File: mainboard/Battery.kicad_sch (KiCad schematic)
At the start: 24 parts, among them IC701 USBLC6-2P6, IC702 BQ21040DBV, IC703 MAX17048, Q701 Si2333CDS, X701 USB, X702 Battery

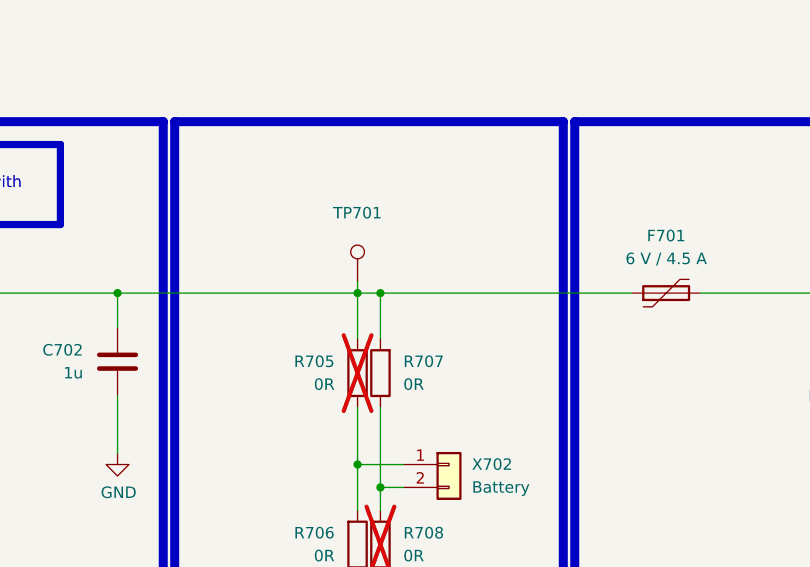
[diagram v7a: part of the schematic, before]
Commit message: Bug: Issue #11
- Add missing name for net for TP701

Closes: #11

Signed-off-by: Daniel Kampert <danielkampert@kampis-elektroecke.de>
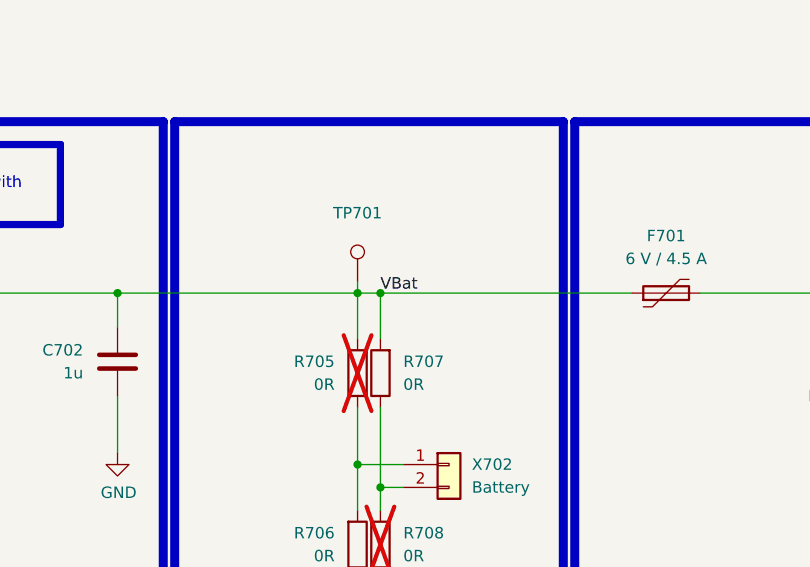
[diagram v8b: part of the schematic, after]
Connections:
- net VBat: now reaches C702.1, F701.1, IC702.2 (OUT), R705.2, R707.2, TP701.1
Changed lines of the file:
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@@
+		)
+	)
+	(label "VBat"
+		(at 232.41 109.22 0)
+		(effects
+			(font
+				(size 1.27 1.27)
+			)
+			(justify left bottom)
 		)
 	)
